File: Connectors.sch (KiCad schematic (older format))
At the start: 33 parts, among them IC4 PJ-002A, J1 691137710002, J2 PRT-16763, J3 691137710002, J4 53048-0810

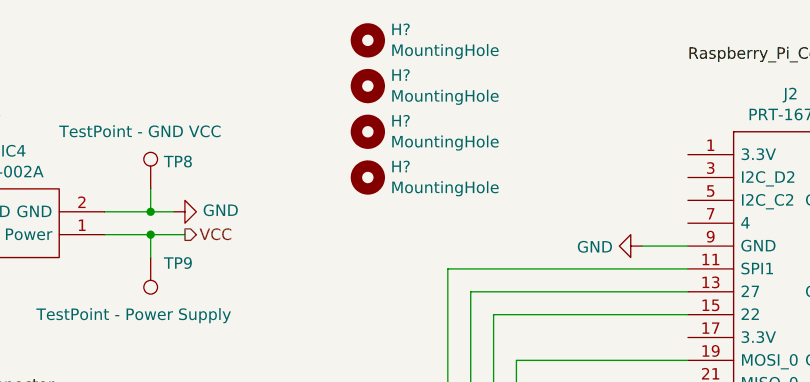
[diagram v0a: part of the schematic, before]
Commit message: Fixed unconnected parts
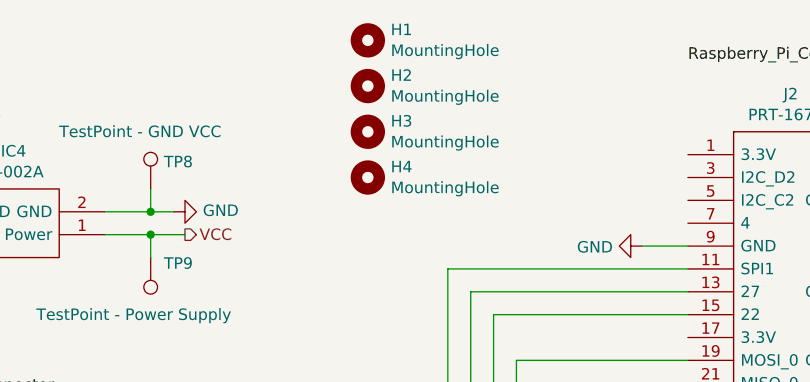
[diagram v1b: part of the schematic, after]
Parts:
- gave numbers to parts that had none: 4
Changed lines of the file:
@@
 	9750 2150 9500 2150
 $Comp
-L Mechanical:MountingHole H?
+L Mechanical:MountingHole H4
 U 1 1 617417BD
 P 3100 1300
-F 0 "H?" H 3200 1346 50  0000 L CNN
+F 0 "H4" H 3200 1346 50  0000 L CNN
 F 1 "MountingHole" H 3200 1255 50  0000 L CNN
 F 2 "MountingHole:MountingHole_2.7mm_M2.5_Pad" H 3100 1300 50  0001 C CNN
@@
 $EndComp
 $Comp
-L Mechanical:MountingHole H?
+L Mechanical:MountingHole H3
 U 1 1 6174245A
 P 3100 1100
-F 0 "H?" H 3200 1146 50  0000 L CNN
+F 0 "H3" H 3200 1146 50  0000 L CNN
 F 1 "MountingHole" H 3200 1055 50  0000 L CNN
 F 2 "MountingHole:MountingHole_2.7mm_M2.5_Pad" H 3100 1100 50  0001 C CNN
@@
 $EndComp
 $Comp
-L Mechanical:MountingHole H?
+L Mechanical:MountingHole H2
 U 1 1 617426E0
 P 3100 900
-F 0 "H?" H 3200 946 50  0000 L CNN
+F 0 "H2" H 3200 946 50  0000 L CNN
 F 1 "MountingHole" H 3200 855 50  0000 L CNN
 F 2 "MountingHole:MountingHole_2.7mm_M2.5_Pad" H 3100 900 50  0001 C CNN
@@
 $EndComp
 $Comp
-L Mechanical:MountingHole H?
+L Mechanical:MountingHole H1
 U 1 1 617428AC
 P 3100 700
-F 0 "H?" H 3200 746 50  0000 L CNN
+F 0 "H1" H 3200 746 50  0000 L CNN
 F 1 "MountingHole" H 3200 655 50  0000 L CNN
 F 2 "MountingHole:MountingHole_2.7mm_M2.5_Pad" H 3100 700 50  0001 C CNN
